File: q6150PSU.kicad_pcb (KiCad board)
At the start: 2 copper layers, 22 parts, among them P1 Vin, P2 Vout, Q1 Q_NMOS_GSD, T1 TRANSFO, U1 LM3478

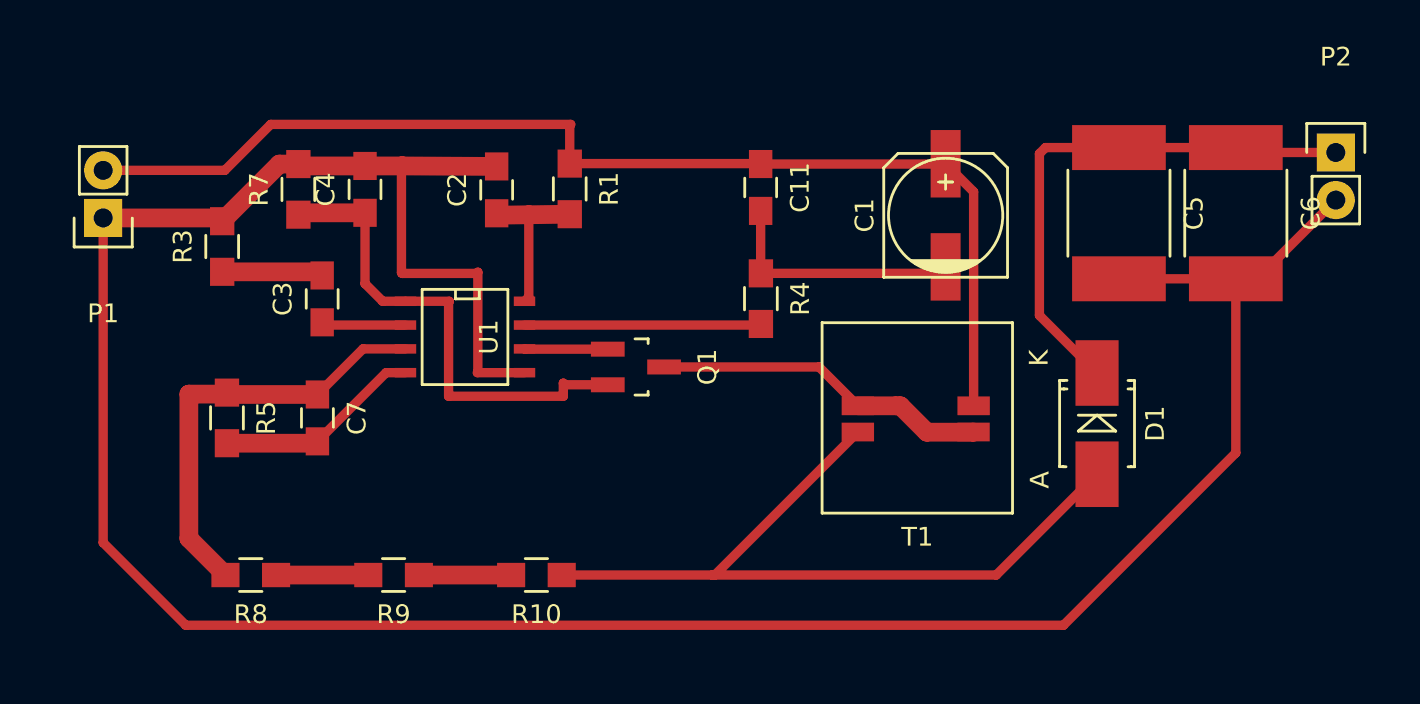
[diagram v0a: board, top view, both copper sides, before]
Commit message: All layout + Pot
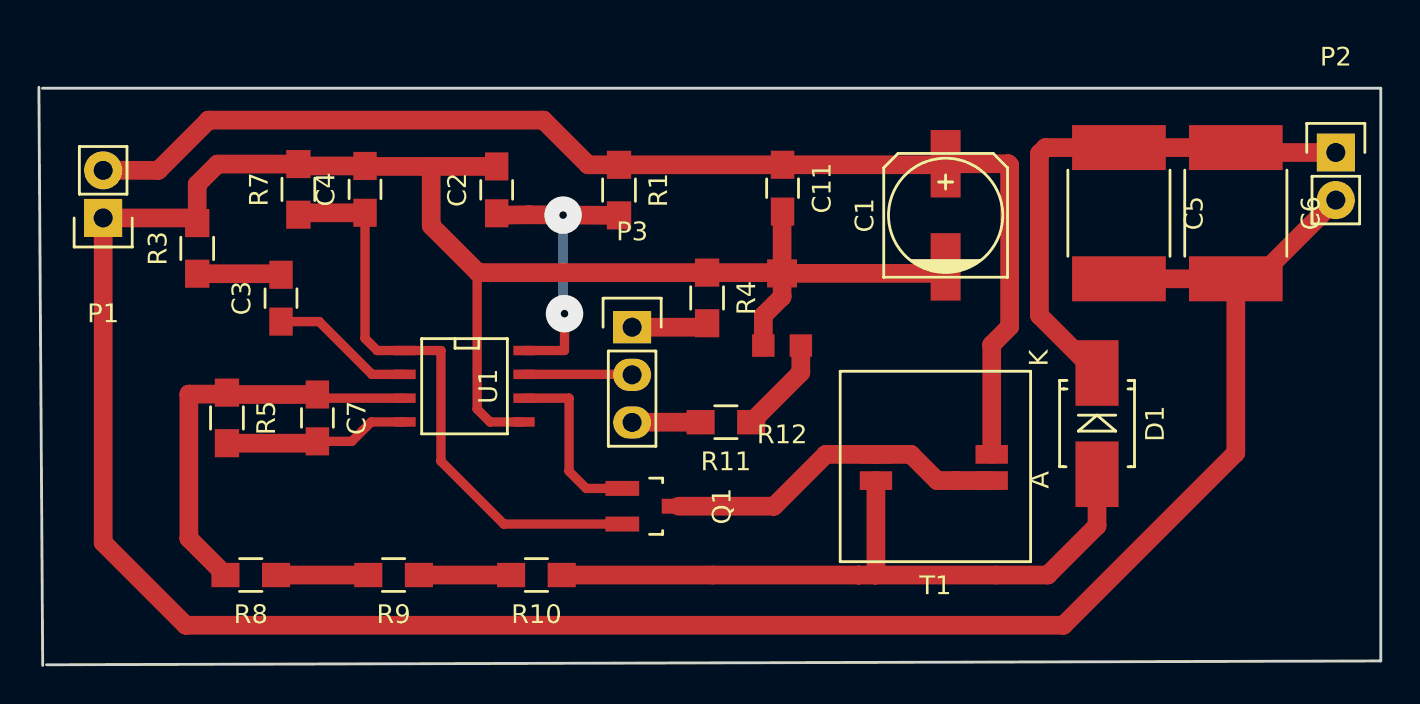
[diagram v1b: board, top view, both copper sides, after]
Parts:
- added P3: CONN_01X03, Pin_Headers:Pin_Header_Straight_1x03, F.Cu at (138.5, 84.6)
- added R11: 12K, Resistors_SMD:R_0805_HandSoldering, F.Cu at (143.5, 89.6)
- added R12: RVAR, BamboulabFootprints:potsmd, F.Cu at (146.5, 83.9)
- moved Q1 7.47 mm to (139.4, 94.1)
- moved R4 2.87 mm to (142.5, 83.0)
- moved T1 2.76 mm to (154.6, 92.0)
- moved R1 2.63 mm to (137.8, 77.3)
- moved U1 2.63 mm to (129.5, 87.7)
- moved C3 2.20 mm to (119.7, 83.0)
- moved R3 1.34 mm to (115.3, 80.4)
- moved C11 1.17 mm to (146.5, 77.2)
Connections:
- R4 pad 2: Net-(R4-Pad2) -> Net-(P3-Pad1)
- U1 pad 7: Net-(R4-Pad2) -> Net-(P3-Pad2)
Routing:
- net GND: track 171.1 -> 190.4 mm
- net Net-(R4-Pad2): track 12.6 -> 0.00 mm
- net Net-(C2-Pad1): track 8.65 -> 16.0 mm, vias 0 -> 2
- net Net-(P3-Pad2): track 0.00 -> 5.78 mm
- net Net-(R11-Pad1): track 0.00 -> 5.20 mm
- net Net-(Q1-Pad1): track 4.45 -> 9.52 mm
- net Net-(C4-Pad1): track 26.6 -> 31.6 mm
- net Net-(C1-Pad1): track 61.7 -> 66.4 mm
- net Net-(D1-Pad2): track 41.7 -> 37.4 mm
- net Net-(P3-Pad1): track 0.00 -> 4.09 mm
- net Net-(C3-Pad1): track 4.51 -> 8.46 mm
- net Net-(P3-Pad3): track 0.00 -> 3.66 mm
- net Net-(C7-Pad1): track 23.1 -> 22.2 mm
- net Net-(C3-Pad2): track 5.41 -> 4.77 mm
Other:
- board outline added: 71.6 x 30.8 mm
- net class Default: trace_width 0.5 -> 1; via_dia 0.6 -> 2

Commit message: Fixed and it works!
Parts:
- moved T1 2.60 mm to (154.9, 89.4), turned to 90 degrees
- moved D1 0.67 mm to (163.9, 89.6)
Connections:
- R10 pad 1: Net-(D1-Pad2) -> Net-(C5-Pad1)
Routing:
- net Net-(C5-Pad1): track 29.0 -> 75.2 mm
- net Net-(D1-Pad2): track 37.4 -> 8.42 mm
- net Net-(C1-Pad1): track 66.4 -> 62.8 mm
- net Net-(Q1-Pad3): track 18.4 -> 21.3 mm
- net GND: track 190.4 -> 192.5 mm
